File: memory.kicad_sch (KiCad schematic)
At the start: 29 parts, among them U10 TPS2117DRLR, U2 SDINBDG4-8G, U9 TPS2117DRLR

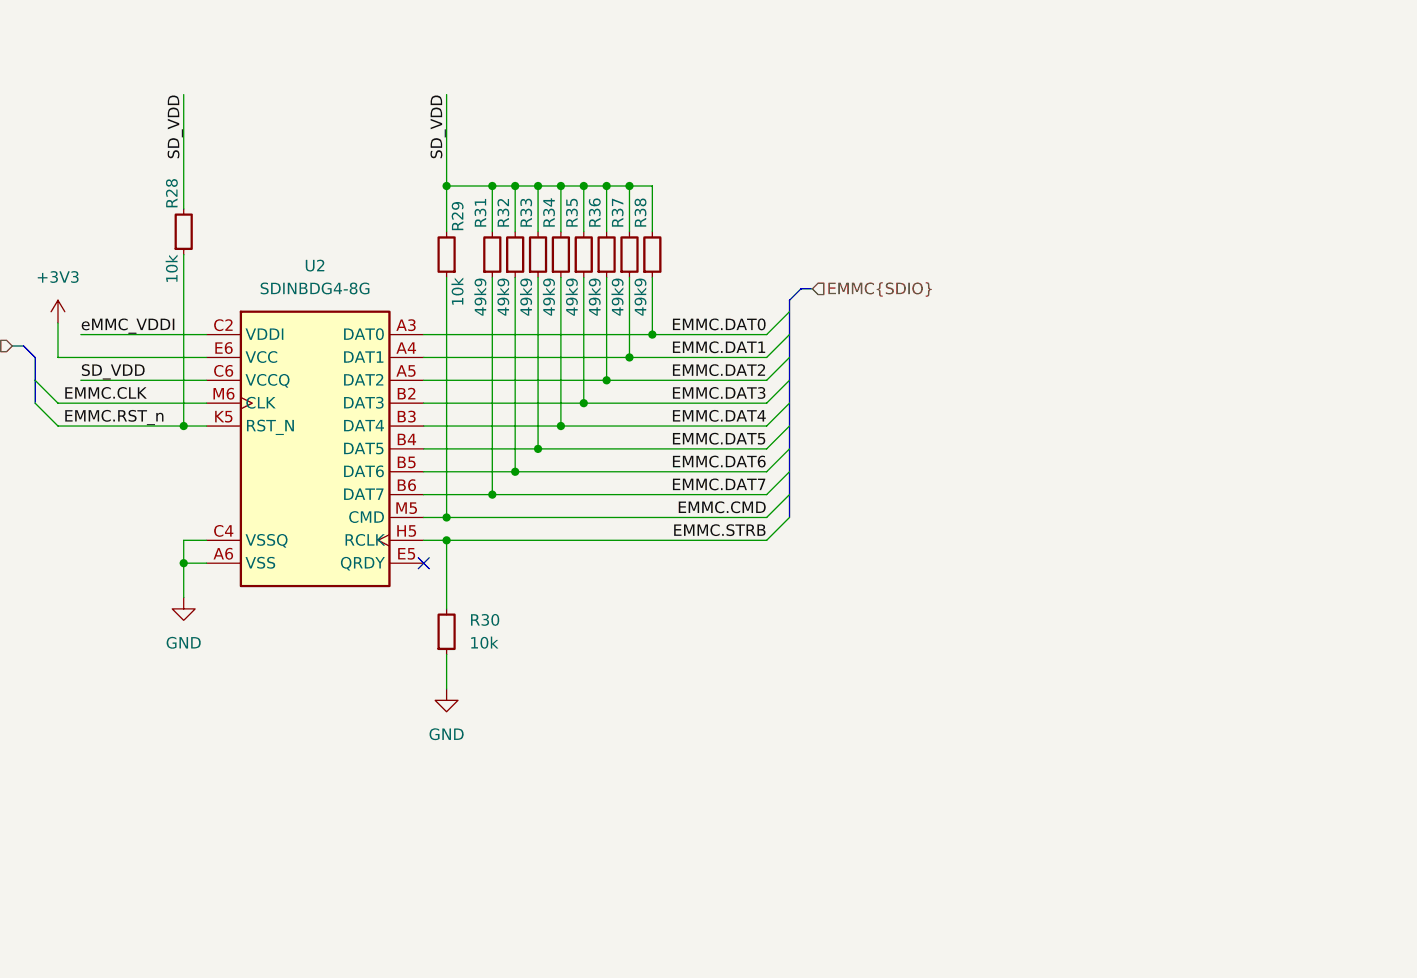
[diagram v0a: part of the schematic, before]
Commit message: [#80745] HDMI DC coupling, KiCAD 9 bump + DRC fixes
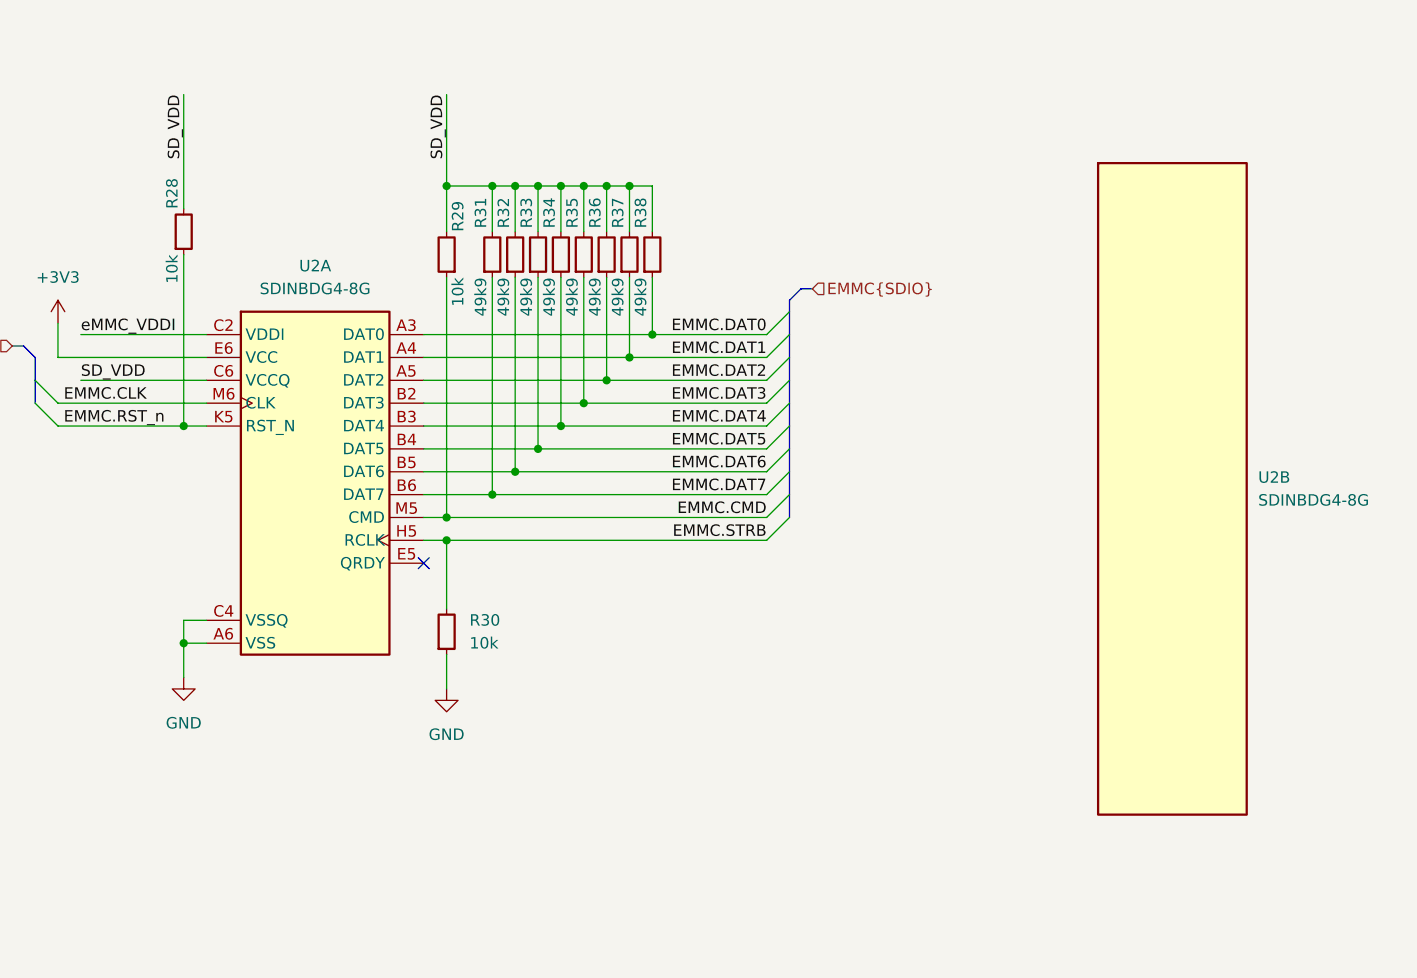
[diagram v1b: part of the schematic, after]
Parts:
- added unit 2 of U2
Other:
- moved on the sheet: U2A

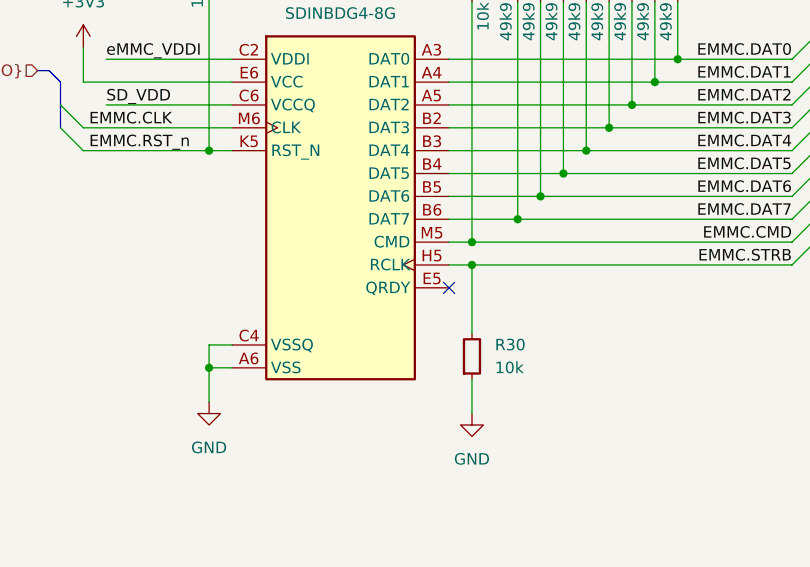
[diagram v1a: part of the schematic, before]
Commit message: [#80745] Update SDINBDG4-8G symbol on schematic, clean ERC
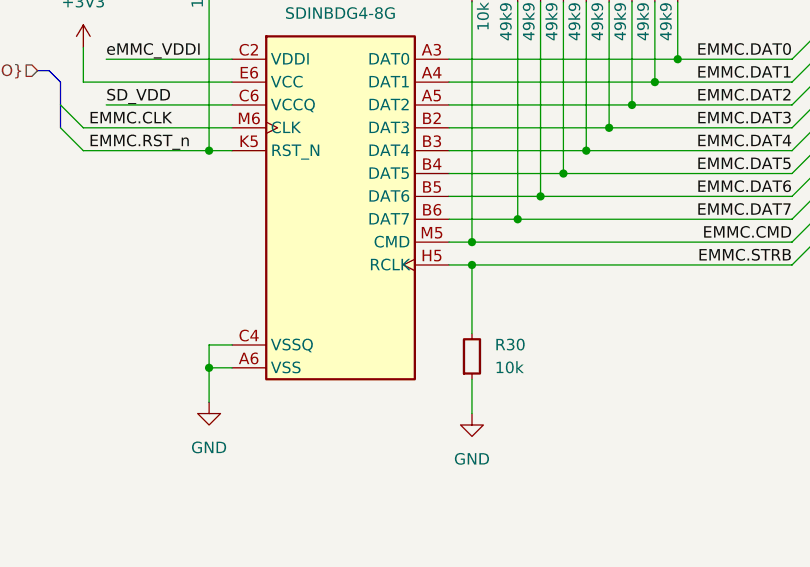
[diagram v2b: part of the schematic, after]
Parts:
- U2: VSD_class (none) -> eMMC
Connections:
- no-connect marks 2 -> 1
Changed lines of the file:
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@@
 	)
 	(no_connect
-		(at 229.87 114.3)
-	)
-	(no_connect
 		(at 83.82 234.95)
 	)
@@
 		(pin "D13"
 		)
-		(pin "E5"
-		)
 		(pin "B1"
 		)
@@
 	)
 	(symbol
-		(lib_name "SDINBDG4-8G_2")
 		(lib_id "antmicroMemory:SDINBDG4-8G")
 		(at 304.8 67.31 0)
@@
 			)
 		)
+		(property "VSD_class" "eMMC"
+			(at 342.9 85.09 0)
+			(effects
+				(font
+					(size 1.27 1.27)
+					(thickness 0.15)
+				)
+				(justify left bottom)
+				(hide yes)
+			)
+		)
 		(pin "N10"
 		)
@@
 		(pin "K7"
 		)
-		(pin "E5"
-		)
 		(pin "H13"
